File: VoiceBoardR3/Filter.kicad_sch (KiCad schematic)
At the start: 36 parts, among them Q301 BC858, Q302 BC858, U301 TL074, U302 MCP45HV51-ST, U303 LM13700

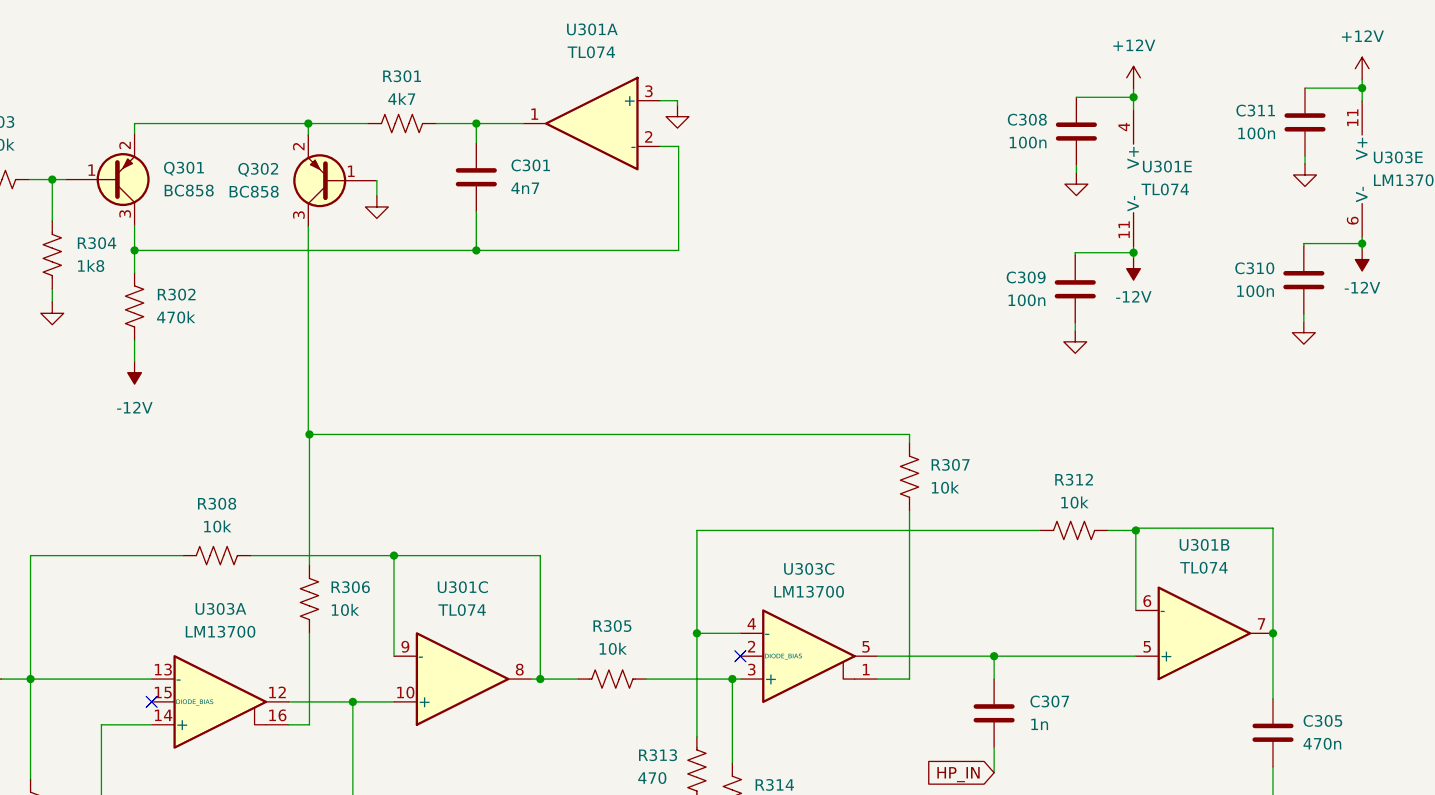
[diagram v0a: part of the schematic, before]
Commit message: updated to kicad 8
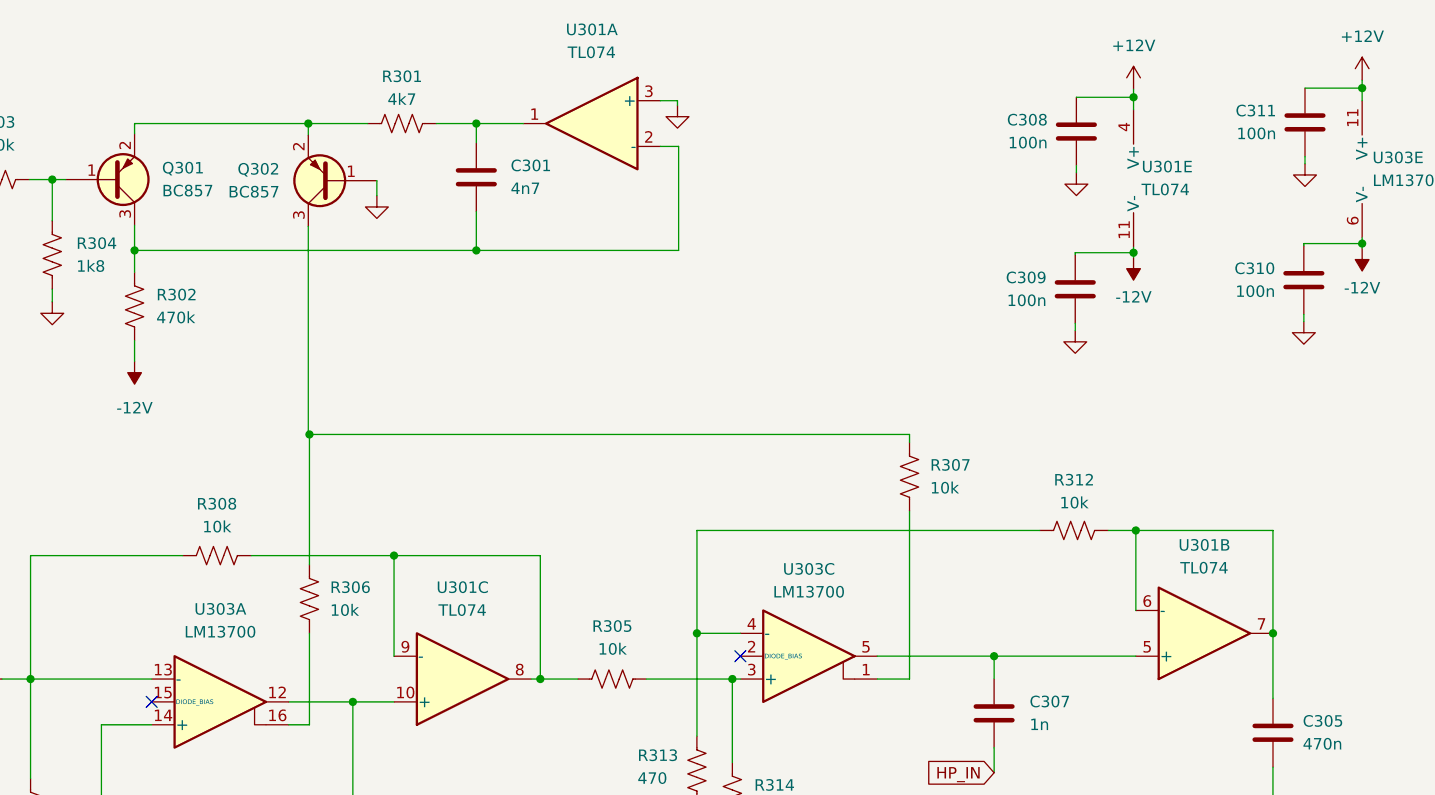
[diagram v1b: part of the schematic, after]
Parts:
- Q301, Q302: value BC858 -> BC857
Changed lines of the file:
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@@
-    (stroke (width 0) (type default))
-  )
-  (wire (pts (xy 169.164 72.898) (xy 169.164 72.644))
     (stroke (width 0) (type default))
   )
@@
     (stroke (width 0) (type default))
   )
-  (wire (pts (xy 169.164 72.644) (xy 184.404 72.644))
+  (wire (pts (xy 169.164 72.898) (xy 184.404 72.898))
     (stroke (width 0) (type default))
   )
@@
     (stroke (width 0) (type default))
   )
-  (wire (pts (xy 184.404 72.644) (xy 184.404 84.328))
+  (wire (pts (xy 184.404 72.898) (xy 184.404 84.328))
     (stroke (width 0) (type default))
   )
@@
       (effects (font (size 1.27 1.27)) (justify left))
     )
-    (property "Value" "BC858" (at 74.041 35.306 0)
+    (property "Value" "BC857" (at 74.041 35.306 0)
       (effects (font (size 1.27 1.27)) (justify left))
     )
@@
   (symbol (lib_id "PCM_Transistor_BJT_AKL:BC858") (at 55.372 33.909 0) (unit 1)
     (in_bom yes) (on_board yes) (dnp no) (fields_autoplaced)
-    (property "Reference" "Q301" (at 61.087 32.639 0)
-      (effects (font (size 1.27 1.27)) (justify left))
-    )
-    (property "Value" "BC858" (at 61.087 35.179 0)
-      (effects (font (size 1.27 1.27)) (justify left))
-    )
+    (property "Reference" "Q301" (at 60.96 32.639 0)
+      (effects (font (size 1.27 1.27)) (justify left))
+    )
+    (property "Value" "BC857" (at 60.96 35.179 0)
+      (effects (font (size 1.27 1.27)) (justify left))
+    )

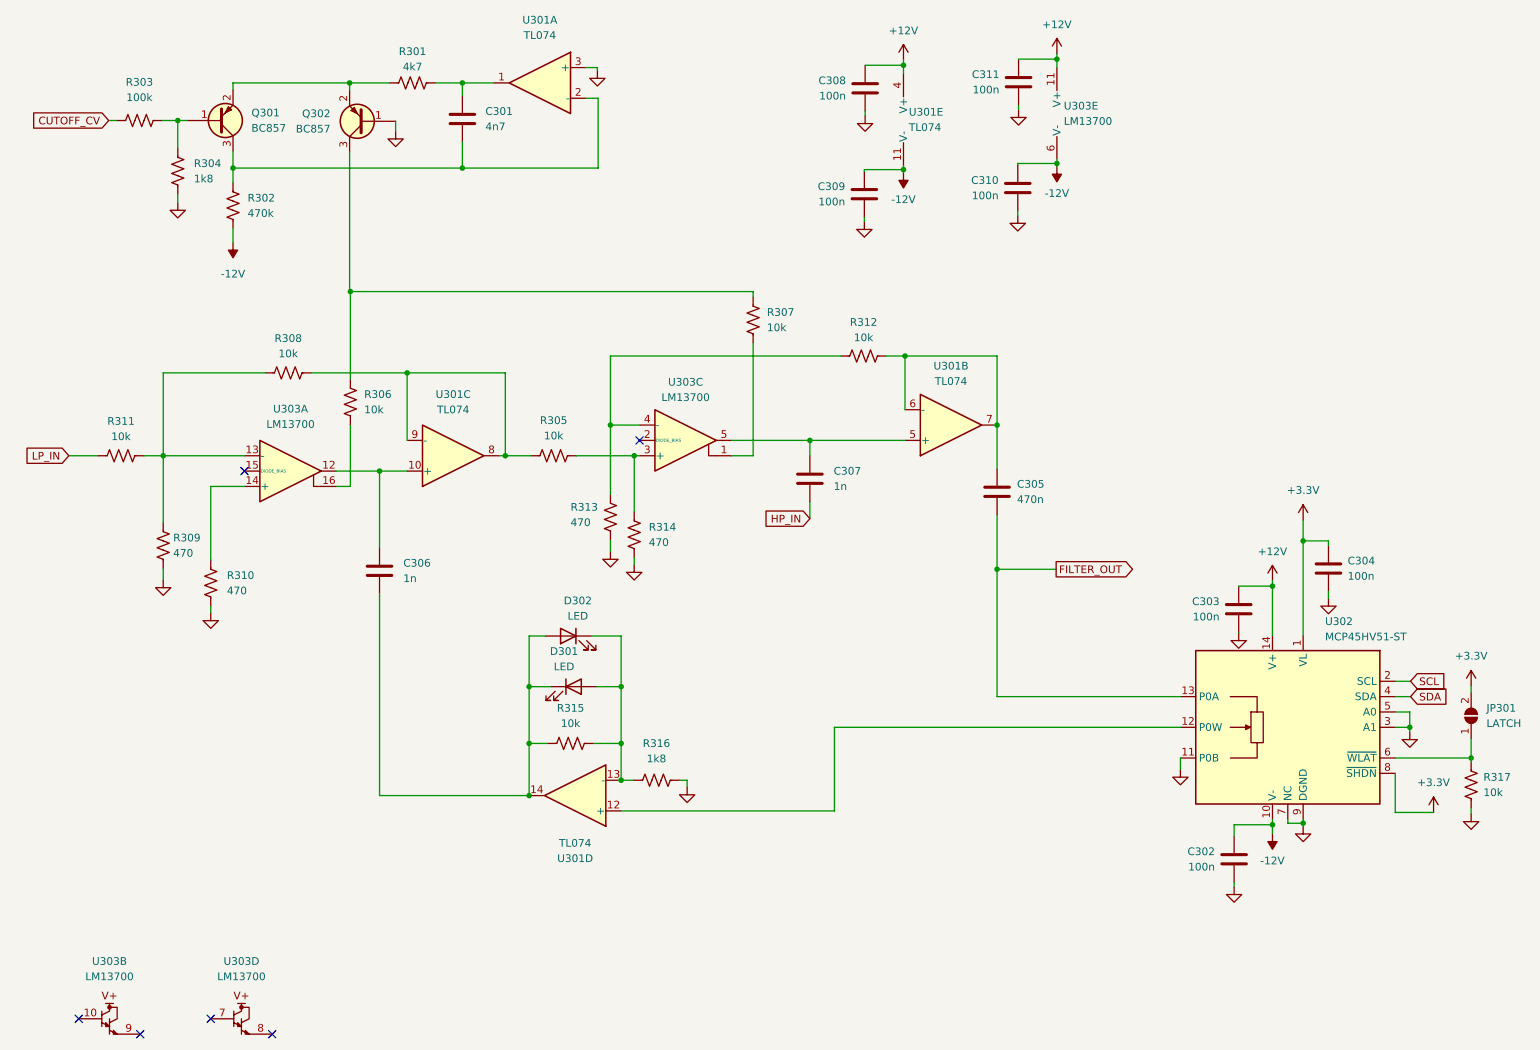
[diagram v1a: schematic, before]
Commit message: separate power supply board
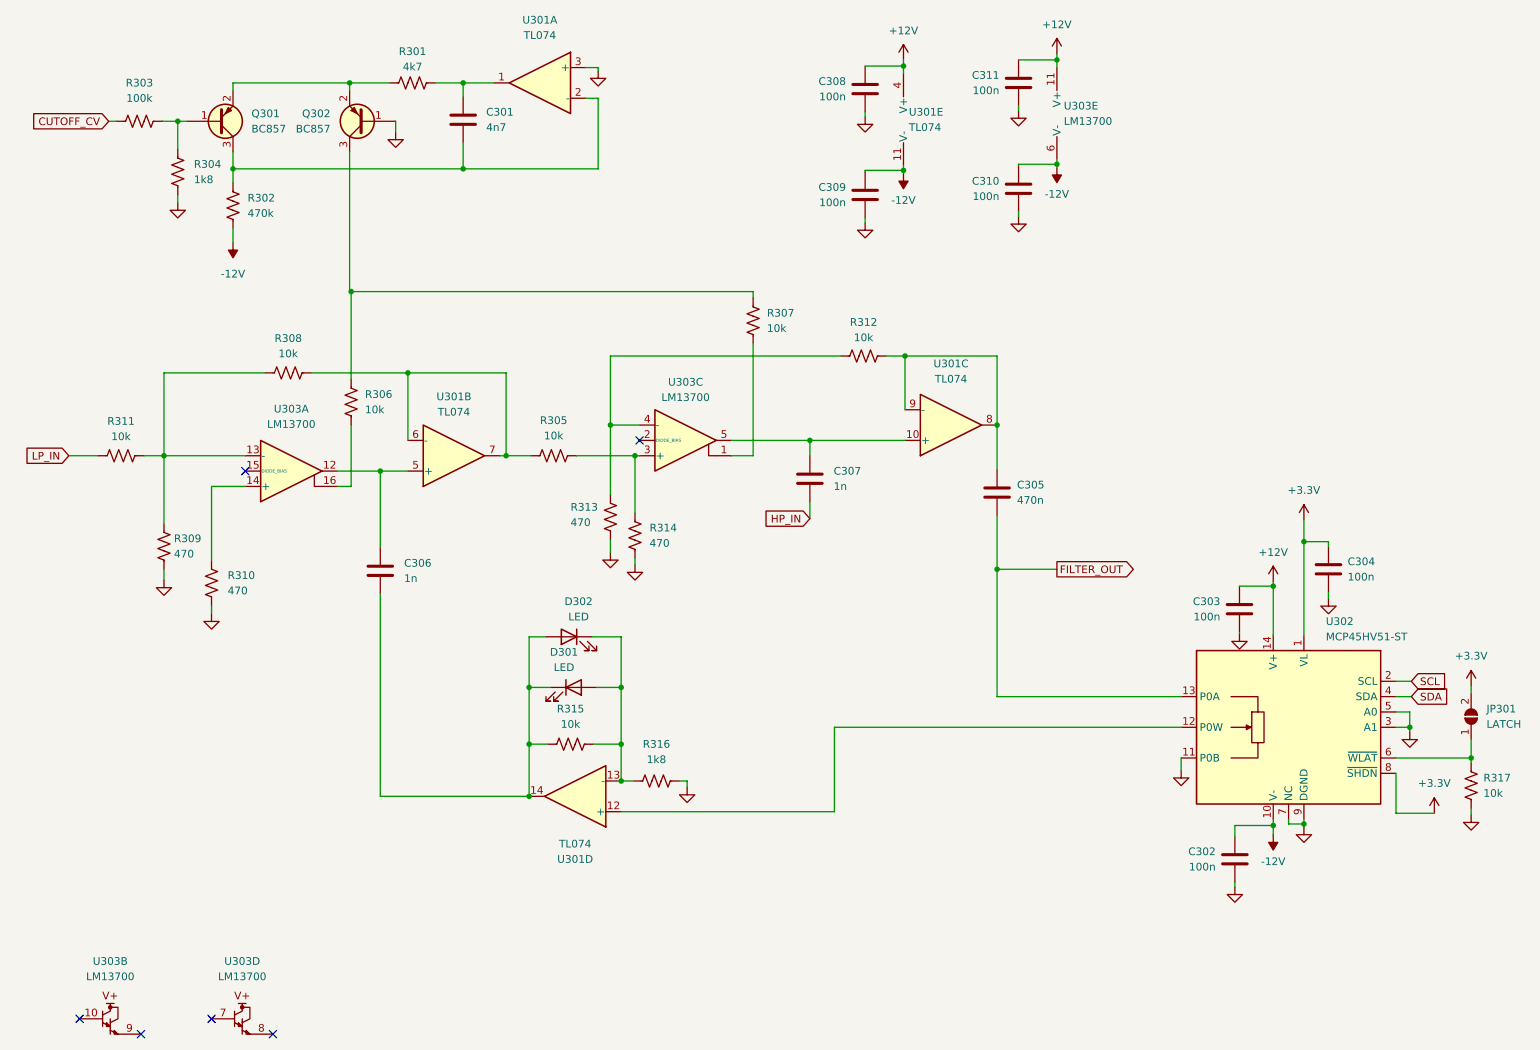
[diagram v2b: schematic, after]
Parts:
- Q301, Q302: footprint PCM_Package_TO_SOT_SMD_AKL:SOT-23 -> PCM_4ms_Package_SOT:SOT-23
- R301, R302, R303, R304, R305, R306, R307, R308, R309, R310, R311, R312, R313, R314, R315, R316, R317: footprint PCM_Resistor_SMD_AKL:R_0805_2012Metric -> Resistor_SMD:R_0805_2012Metric
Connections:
- net at C306.1, U303.12: now also U301.5 (+); no longer U301.10 (+)
- net at C305.1, R312.2: now also U301.8, U301.9 (-); no longer U301.6 (-), U301.7
- net at R305.2, R308.2: now also U301.6 (-), U301.7; no longer U301.8, U301.9 (-)
- net at C307.1, U303.5: now also U301.10 (+); no longer U301.5 (+)
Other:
- moved on the sheet: U301B, U301C
